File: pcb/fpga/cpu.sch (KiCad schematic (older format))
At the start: 52 parts, among them CON1 USB-MINI-B, P1 BANK1, P2 BANK2, P3 CONN_6, P4 BANK3, P5 BANK4, U1 EPCS1, U2 EP1C3T100, U3 BA15BC0FP-E2_-_LDO, U4 LM1084IS-3.3/NOPB

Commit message: fpga pcb - add part details
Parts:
- D1: Farnell (none) -> http://il.farnell.com/dialight/5988150107f/led-yellow-1-25m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; PARTNO (none) -> 5988150107F
- OSC1: Farnell (none) -> http://il.farnell.com/silicon-labs/501aaa50m0000daf/osc-50m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; PARTNO (none) -> 501AAA50M0000DAF
- RP1: Farnell (none) -> http://il.farnell.com/yageo/yc164-jr-0710kl/resistor-iso-ar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; PARTNO (none) -> YC164-JR-0710KL
- RP2: Farnell (none) -> http://il.farnell.com/bourns/4116r-1-271lf/resistor-network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; PARTNO (none) -> 4116R-1-271LF
- U1: PARTNO (none) -> EPCS1
- U3: Farnell (none) -> http://il.farnell.com/rohm/ba15bc0fp-e2/ldo-fixed-1-5v-1a-t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; PARTNO (none) -> BA15BC0FP-E2
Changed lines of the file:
@@
 F 1 "EPCS1" H 2950 1450 60  0000 C CNN
 F 2 "" H 2700 1050 60  0000 C CNN
-F 3 "" H 2700 1050 60  0000 C CNN
+F 3 "http://www.altera.com/literature/hb/cfg/cyc_c51014.pdf" H 2700 1050 60  0001 C CNN
+F 4 "EPCS1" H 2700 1050 60  0001 C CNN "PARTNO"
 	1    2700 1050
 	1    0    0    -1
@@
 F 1 "270" H 10950 4350 40  0000 C CNN
 F 2 "" H 10950 4800 60  0000 C CNN
-F 3 "" H 10950 4800 60  0000 C CNN
+F 3 "http://www.farnell.com/datasheets/1695346.pdf" H 10950 4800 60  0000 C CNN
+F 4 "http://il.farnell.com/bourns/4116r-1-271lf/resistor-network-270r/dp/9355910" H 10950 4800 60  0001 C CNN "Farnell"
+F 5 "4116R-1-271LF" H 10950 4800 60  0001 C CNN "PARTNO"
 	1    10950 4800
 	1    0    0    -1
@@
 F 1 "LED" H 9850 3750 50  0000 C CNN
 F 2 "" H 9850 3850 60  0000 C CNN
-F 3 "" H 9850 3850 60  0000 C CNN
+F 3 "http://www.farnell.com/datasheets/1484480.pdf" H 9850 3850 60  0001 C CNN
+F 4 "http://il.farnell.com/dialight/5988150107f/led-yellow-1-25mm-x-1-4mm-130mcd/dp/2369031" H 9850 3850 60  0001 C CNN "Farnell"
+F 5 "5988150107F " H 9850 3850 60  0001 C CNN "PARTNO"
 	1    9850 3850
 	-1   0    0    1
@@
 F 1 "501AAA" H 2150 8150 60  0000 C CNN
 F 2 "" H 2100 7800 60  0000 C CNN
-F 3 "" H 2100 7800 60  0000 C CNN
+F 3 "http://www.farnell.com/datasheets/1792138.pdf" H 2100 7800 60  0001 C CNN
+F 4 "http://il.farnell.com/silicon-labs/501aaa50m0000daf/osc-50mhz-50ppm-1-8-3-3v-smd/dp/2394197" H 2150 8000 60  0001 C CNN "Farnell"
+F 5 "501AAA50M0000DAF" H 2150 8000 60  0001 C CNN "PARTNO"
 	1    2150 8000
 	1    0    0    -1
@@
 F 1 "BA15BC0FP-E2_-_LDO" H 10350 1300 40  0000 L CNN
 F 2 "TO-252" H 10350 1200 30  0000 C CIN
-F 3 "" H 10350 1100 60  0000 C CNN
+F 3 "http://www.farnell.com/datasheets/1747234.pdf" H 10350 1100 60  0001 C CNN
+F 4 "http://il.farnell.com/rohm/ba15bc0fp-e2/ldo-fixed-1-5v-1a-to-252-3/dp/2342871" H 10350 1100 60  0001 C CNN "Farnell"
+F 5 "BA15BC0FP-E2" H 10350 1100 60  0001 C CNN "PARTNO"
 	1    10350 1100
 	1    0    0    -1
@@
 F 1 "10K" H 2200 2500 40  0000 C CNN
 F 2 "" H 2200 2550 60  0000 C CNN
-F 3 "" H 2200 2550 60  0000 C CNN
+F 3 "http://www.farnell.com/datasheets/443424.pdf" H 1900 2300 60  0001 C CNN
+F 4 "http://il.farnell.com/yageo/yc164-jr-0710kl/resistor-iso-array-4res-10kohm/dp/2413810" H 2200 2550 60  0001 C CNN "Farnell"
+F 5 "YC164-JR-0710KL" H 2200 2550 60  0001 C CNN "PARTNO"
 	1    2200 2550
 	1    0    0    -1

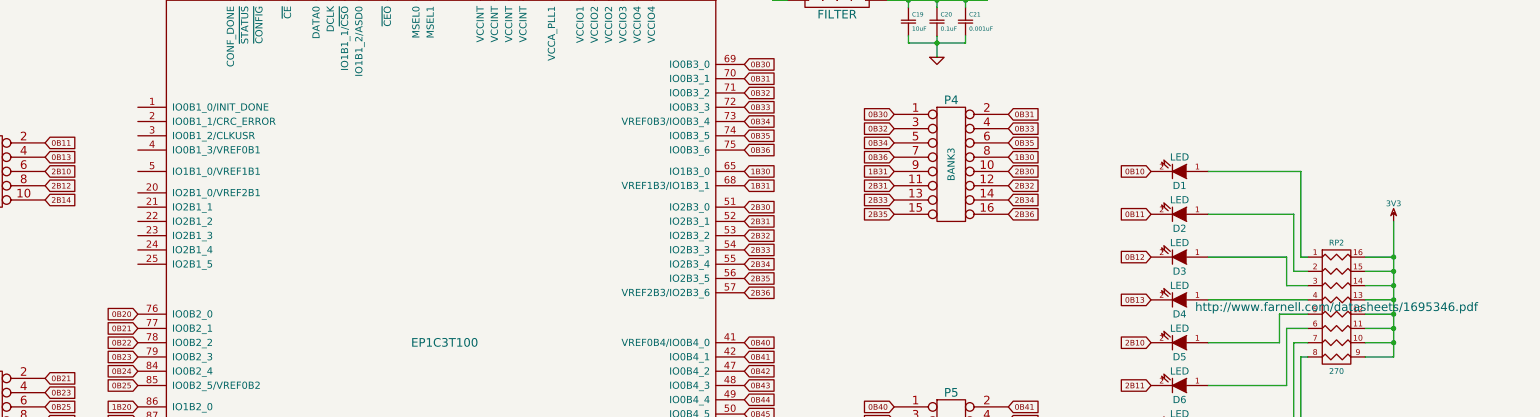
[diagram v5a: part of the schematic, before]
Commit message: fpga pcb - bank 1 header
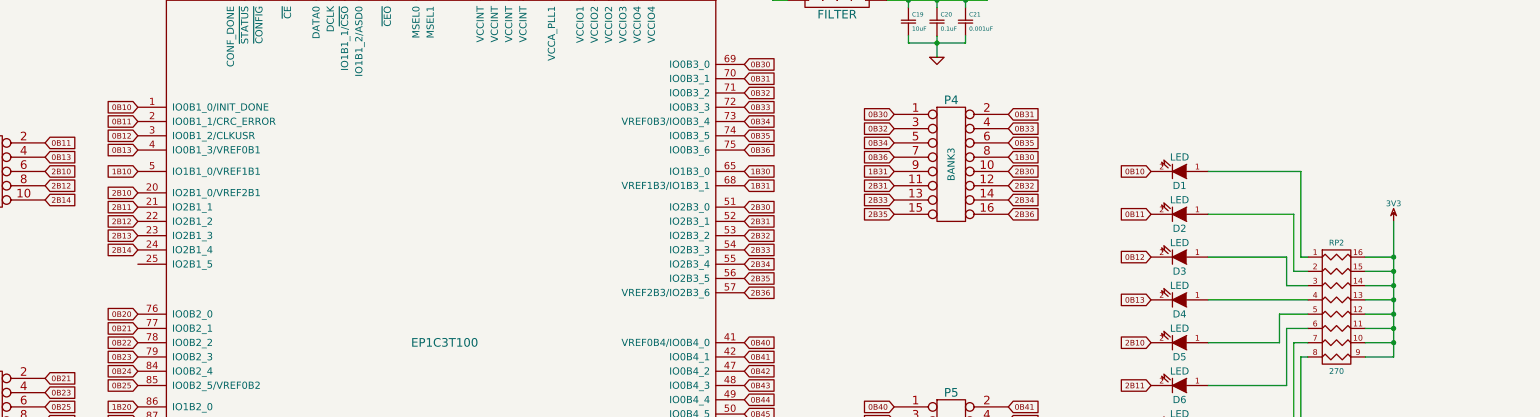
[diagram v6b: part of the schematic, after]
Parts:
- C24, C25: Farnell (none) -> http://il.farnell.com/panasonic-electronic-components/eeefk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; PARTNO (none) -> EEEFK0J102AP
- FB1, FB2: Farnell (none) -> http://il.farnell.com/tdk/mmz2012202bt000/ferrite-bead-0-5o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; PARTNO (none) -> MMZ2012Y202BT000
- U2: Farnell (none) -> http://il.farnell.com/altera/ep1c3t100c8n/ic-cyclone-fpga-2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; PARTNO (none) -> EP1C3T100C8N; Pinout (none) -> http://www.altera.com/literature/dp/cyclone/ep1c3t100.pdf
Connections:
- net 0B10: now also U2.1 (IO0B1_0/INIT_DONE)
- net 0B11: now also U2.2 (IO0B1_1/CRC_ERROR)
- net 0B12: now also U2.3 (IO0B1_2/CLKUSR)
- net 0B13: now also U2.4 (IO0B1_3/VREF0B1)
- net 1B10: now also U2.5 (IO1B1_0/VREF1B1)
- net 2B10: now also U2.20 (IO2B1_0/VREF2B1)
- net 2B11: now also U2.21 (IO2B1_1)
- net 2B12: now also U2.22 (IO2B1_2)
- net 2B13: now also U2.23 (IO2B1_3)
- net 2B14: now also U2.24 (IO2B1_4)
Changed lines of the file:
@@
 F 1 "EP1C3T100" H 4700 5050 60  0000 C CNN
 F 2 "" H 3150 7700 60  0000 C CNN
-F 3 "" H 3150 7700 60  0000 C CNN
+F 3 "http://www.farnell.com/datasheets/5080.pdf" H 3150 7700 60  0001 C CNN
+F 4 "http://il.farnell.com/altera/ep1c3t100c8n/ic-cyclone-fpga-2910-smd-1c3t100/dp/1453501" H 4700 5050 60  0001 C CNN "Farnell"
+F 5 "EP1C3T100C8N " H 4700 5050 60  0001 C CNN "PARTNO"
+F 6 "http://www.altera.com/literature/dp/cyclone/ep1c3t100.pdf" H 4700 5050 60  0001 C CNN "Pinout"
 	1    4700 5050
 	1    0    0    -1
@@
 F 1 "1000uF" H 10756 2065 40  0000 L CNN
 F 2 "" H 10788 2000 30  0000 C CNN
-F 3 "" H 10750 2150 60  0000 C CNN
+F 3 "http://www.farnell.com/datasheets/58258.pdf" H 10750 2150 60  0001 C CNN
+F 4 "EEEFK0J102AP " H 10750 2150 60  0001 C CNN "PARTNO"
+F 5 "http://il.farnell.com/panasonic-electronic-components/eeefk0j102ap/cap-alu-elec-1000uf-6-3v-smd-reel/dp/2254374" H 10750 2150 60  0001 C CNN "Farnell"
 	1    10750 2150
 	1    0    0    -1
@@
 F 1 "270" H 10950 4350 40  0000 C CNN
 F 2 "" H 10950 4800 60  0000 C CNN
-F 3 "http://www.farnell.com/datasheets/1695346.pdf" H 10950 4800 60  0000 C CNN
+F 3 "http://www.farnell.com/datasheets/1695346.pdf" H 10950 4800 60  0001 C CNN
 F 4 "http://il.farnell.com/bourns/4116r-1-271lf/resistor-network-270r/dp/9355910" H 10950 4800 60  0001 C CNN "Farnell"
 F 5 "4116R-1-271LF" H 10950 4800 60  0001 C CNN "PARTNO"
@@
 F 1 "1000uF" H 10756 1215 40  0000 L CNN
 F 2 "" H 10788 1150 30  0000 C CNN
-F 3 "" H 10750 1300 60  0000 C CNN
+F 3 "http://www.farnell.com/datasheets/58258.pdf" H 10750 1300 60  0001 C CNN
+F 4 "http://il.farnell.com/panasonic-electronic-components/eeefk0j102ap/cap-alu-elec-1000uf-6-3v-smd-reel/dp/2254374" H 10750 1300 60  0001 C CNN "Farnell"
+F 5 "EEEFK0J102AP " H 10750 1300 60  0001 C CNN "PARTNO"
 	1    10750 1300
 	1    0    0    -1
@@
 F 1 "FILTER" H 7450 2550 60  0000 C CNN
 F 2 "" H 7450 2650 60  0000 C CNN
-F 3 "" H 7450 2650 60  0000 C CNN
+F 3 "http://www.farnell.com/datasheets/712877.pdf" H 7450 2650 60  0001 C CNN
+F 4 "http://il.farnell.com/tdk/mmz2012202bt000/ferrite-bead-0-5ohm-400ma-0805/dp/2372958" H 7450 2650 60  0001 C CNN "Farnell"
+F 5 "MMZ2012Y202BT000 " H 7450 2650 60  0001 C CNN "PARTNO"
 	1    7450 2650
 	1    0    0    -1
@@
 F 1 "FILTER" H 9200 1900 60  0000 C CNN
 F 2 "" H 9200 2000 60  0000 C CNN
-F 3 "" H 9200 2000 60  0000 C CNN
+F 3 "http://www.farnell.com/datasheets/712877.pdf" H 9200 2000 60  0001 C CNN
+F 4 "http://il.farnell.com/tdk/mmz2012202bt000/ferrite-bead-0-5ohm-400ma-0805/dp/2372958" H 9200 2000 60  0001 C CNN "Farnell"
+F 5 "MMZ2012Y202BT000 " H 9200 2000 60  0001 C CNN "PARTNO"
 	1    9200 2000
 	1    0    0    -1
@@
 Text GLabel 1750 8000 0    39   Input ~ 0
 OSC_OE
+Text GLabel 2550 3400 0    39   Input ~ 0
+0B10
+Text GLabel 2550 3500 0    39   Input ~ 0
+0B11
+Text GLabel 2550 3600 0    39   Input ~ 0
+0B12
+Text GLabel 2550 3700 0    39   Input ~ 0
+0B13
+Text GLabel 2550 3850 0    39   Input ~ 0
+1B10
+Text GLabel 2550 4000 0    39   Input ~ 0
+2B10
+Text GLabel 2550 4100 0    39   Input ~ 0
+2B11
+Text GLabel 2550 4200 0    39   Input ~ 0
+2B12
+Text GLabel 2550 4300 0    39   Input ~ 0
+2B13
+Text GLabel 2550 4400 0    39   Input ~ 0
+2B14
 $EndSCHEMATC

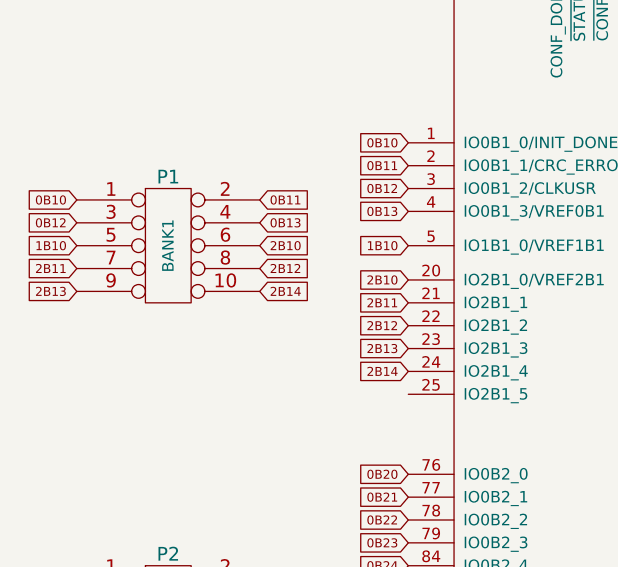
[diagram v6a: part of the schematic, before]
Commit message: fpga pcb - fix bank 1
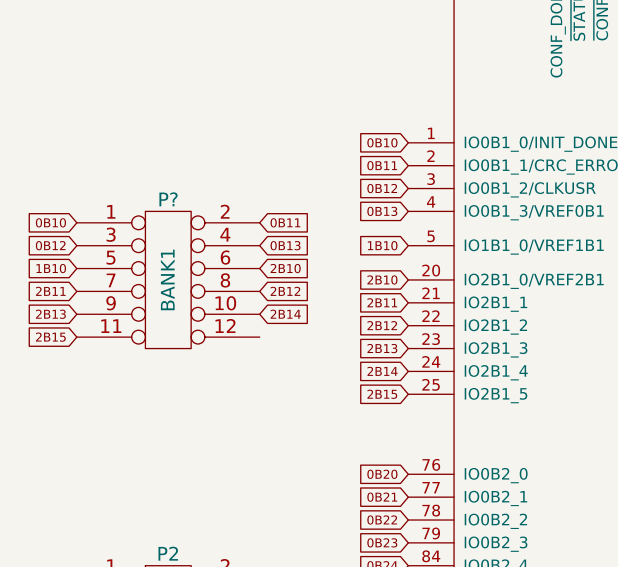
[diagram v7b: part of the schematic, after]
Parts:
- removed P1: BANK1, symbol CONN_5X2
- added P?: BANK1, symbol CONN_6X2
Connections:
- net 0B10: now also P?.1 (P1)
- net 0B11: now also P?.2 (P2)
- net 0B12: now also P?.3 (P3)
- net 0B13: now also P?.4 (P4)
- net 1B10: now also P?.5 (P5)
- net 2B10: now also P?.6 (P6)
- net 2B11: now also P?.7 (P7)
- net 2B12: now also P?.8 (P8)
- net 2B13: now also P?.9
- net 2B14: now also P?.10
- net 2B15: now reaches U2.25 (IO2B1_5)
- net 2B15: now also P?.11
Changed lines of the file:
@@
 Text GLabel 7850 6300 0    39   Input ~ 0
 2B46
-$Comp
-L CONN_5X2 P1
-U 1 1 549CD2BD
-P 1500 3850
-F 0 "P1" H 1500 4150 60  0000 C CNN
-F 1 "BANK1" V 1500 3850 50  0000 C CNN
-F 2 "" H 1500 3850 60  0000 C CNN
-F 3 "" H 1500 3850 60  0000 C CNN
-	1    1500 3850
-	1    0    0    -1
-$EndComp
 Text GLabel 9650 3850 0    39   Input ~ 0
 0B10
@@
 	1    0    0    -1
 $EndComp
-Text GLabel 1100 3650 0    39   Input ~ 0
+Text GLabel 1100 3750 0    39   Input ~ 0
 0B10
-Text GLabel 1900 3650 2    39   Input ~ 0
+Text GLabel 1900 3750 2    39   Input ~ 0
 0B11
-Text GLabel 1100 3750 0    39   Input ~ 0
+Text GLabel 1100 3850 0    39   Input ~ 0
 0B12
-Text GLabel 1900 3750 2    39   Input ~ 0
+Text GLabel 1900 3850 2    39   Input ~ 0
 0B13
-Text GLabel 1100 3850 0    39   Input ~ 0
+Text GLabel 1100 3950 0    39   Input ~ 0
 1B10
-Text GLabel 1900 3850 2    39   Input ~ 0
+Text GLabel 1900 3950 2    39   Input ~ 0
 2B10
-Text GLabel 1100 3950 0    39   Input ~ 0
+Text GLabel 1100 4050 0    39   Input ~ 0
 2B11
-Text GLabel 1900 3950 2    39   Input ~ 0
+Text GLabel 1900 4050 2    39   Input ~ 0
 2B12
-Text GLabel 1100 4050 0    39   Input ~ 0
+Text GLabel 1100 4150 0    39   Input ~ 0
 2B13
-Text GLabel 1900 4050 2    39   Input ~ 0
+Text GLabel 1900 4150 2    39   Input ~ 0
 2B14
 Text GLabel 1100 5300 0    39   Input ~ 0
@@
 Text GLabel 2550 4400 0    39   Input ~ 0
 2B14
+$Comp
+L CONN_6X2 P?
+U 1 1 54ADB017
+P 1500 4000
+F 0 "P?" H 1500 4350 60  0000 C CNN
+F 1 "BANK1" V 1500 4000 60  0000 C CNN
+F 2 "" H 1500 4000 60  0000 C CNN
+F 3 "" H 1500 4000 60  0000 C CNN
+	1    1500 4000
+	1    0    0    -1
+$EndComp
+Text GLabel 2550 4500 0    39   Input ~ 0
+2B15
+Text GLabel 1100 4250 0    39   Input ~ 0
+2B15
 $EndSCHEMATC

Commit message: nim sim improvements
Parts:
- added P6: PWR, symbol CONN_2
- gave numbers to parts that had none: 1
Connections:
- net +1.5V: now also P6.1 (P1)
- net GND: now also P6.2 (PM)
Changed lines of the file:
@@
 $EndComp
 $Comp
-L GND #PWR32
+L GND #PWR34
 U 1 1 549CDE40
 P 10350 2500
-F 0 "#PWR32" H 10350 2500 30  0001 C CNN
+F 0 "#PWR34" H 10350 2500 30  0001 C CNN
 F 1 "GND" H 10350 2430 30  0001 C CNN
 F 2 "" H 10350 2500 60  0000 C CNN
@@
 $EndComp
 $Comp
-L +3.3V #PWR34
+L +3.3V #PWR36
 U 1 1 549CF048
 P 11100 1700
-F 0 "#PWR34" H 11100 1660 30  0001 C CNN
+F 0 "#PWR36" H 11100 1660 30  0001 C CNN
 F 1 "+3.3V" H 11100 1810 30  0000 C CNN
 F 2 "" H 11100 1700 60  0000 C CNN
@@
 $EndComp
 $Comp
-L 3V3 #PWR35
+L 3V3 #PWR37
 U 1 1 54A1E600
 P 11350 4200
-F 0 "#PWR35" H 11350 4300 40  0001 C CNN
+F 0 "#PWR37" H 11350 4300 40  0001 C CNN
 F 1 "3V3" H 11350 4325 40  0000 C CNN
 F 2 "" H 11350 4200 60  0000 C CNN
@@
 $EndComp
 $Comp
-L +1.5V #PWR33
+L +1.5V #PWR35
 U 1 1 54A85D86
 P 11100 900
-F 0 "#PWR33" H 11100 1040 20  0001 C CNN
+F 0 "#PWR35" H 11100 1040 20  0001 C CNN
 F 1 "+1.5V" H 11100 1010 30  0000 C CNN
 F 2 "" H 11100 900 60  0000 C CNN
@@
 $EndComp
 $Comp
-L GND #PWR31
+L GND #PWR33
 U 1 1 54A85EE1
 P 10350 1600
-F 0 "#PWR31" H 10350 1600 30  0001 C CNN
+F 0 "#PWR33" H 10350 1600 30  0001 C CNN
 F 1 "GND" H 10350 1530 30  0001 C CNN
 F 2 "" H 10350 1600 60  0000 C CNN
@@
 2B14
 $Comp
-L CONN_6X2 P?
+L CONN_6X2 P1
 U 1 1 54ADB017
 P 1500 4000
-F 0 "P?" H 1500 4350 60  0000 C CNN
+F 0 "P1" H 1500 4350 60  0000 C CNN
 F 1 "BANK1" V 1500 4000 60  0000 C CNN
 F 2 "" H 1500 4000 60  0000 C CNN
@@
 Text GLabel 1100 4250 0    39   Input ~ 0
 2B15
+$Comp
+L CONN_2 P6
+U 1 1 55025AED
+P 9750 2950
+F 0 "P6" V 9700 2950 40  0000 C CNN
+F 1 "PWR" V 9800 2950 40  0000 C CNN
+F 2 "" H 9750 2950 60  0000 C CNN
+F 3 "" H 9750 2950 60  0000 C CNN
+	1    9750 2950
+	1    0    0    -1
+$EndComp
+$Comp
+L +3.3V #PWR31
+U 1 1 55025DFE
+P 9300 2750
+F 0 "#PWR31" H 9300 2710 30  0001 C CNN
+F 1 "+3.3V" H 9300 2860 30  0000 C CNN
+F 2 "" H 9300 2750 60  0000 C CNN
+F 3 "" H 9300 2750 60  0000 C CNN
+	1    9300 2750
+	1    0    0    -1
+$EndComp
+$Comp
+L GND #PWR32
+U 1 1 5502643F
+P 9300 3200
+F 0 "#PWR32" H 9300 3200 30  0001 C CNN
+F 1 "GND" H 9300 3130 30  0001 C CNN
+F 2 "" H 9300 3200 60  0000 C CNN
+F 3 "" H 9300 3200 60  0000 C CNN
+	1    9300 3200
+	1    0    0    -1
+$EndComp
+Wire Wire Line
+	9400 2850 9300 2850
+Wire Wire Line
+	9300 2850 9300 2750
+Wire Wire Line
+	9400 3050 9300 3050
+Wire Wire Line
+	9300 3050 9300 3200
 $EndSCHEMATC
